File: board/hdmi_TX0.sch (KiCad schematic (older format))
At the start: 21 parts

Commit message: Update from the template.
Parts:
- CTX001, CTX002, CTX003, CTX004, CTX005, CTX006, CTX007, CTX008, CTX016, CTX017: value 100n -> 0.1uF
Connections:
- net HDMI_TX0_EQ0: now also PTX0.9 (P9); no longer PTX0.3 (P3)
- net HDMI_TX0_EQ1: now also PTX0.3 (P3); no longer PTX0.9 (P9)
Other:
- note added: "This sheet is generated from ../external/templates/\nDO NOT MODIFY!!!\n1620b96"
- note removed: "This sheet is generated from ../external/templates/\nDO NOT MODIFY!!!\nee70a4a"
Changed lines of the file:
@@
 LIBS:contrib
 LIBS:valves
-LIBS:pmod
+LIBS:pmod-conn_6x2
+LIBS:ma78l00
 LIBS:hdmi
 LIBS:ptn3363
-LIBS:ma78l00
-LIBS:pmod-conn_6x2
-LIBS:EEPROM
-LIBS:xc9140
-LIBS:reg710-dbv
-LIBS:pmod-hdmi-tx-cache
 EELAYER 25 0
 EELAYER END
 $Descr A3 16535 11693
 encoding utf-8
-Sheet 1 2
+Sheet 1 1
 Title ""
 Date ""
@@
 U 1 1 57C07746
 P 7450 5400
-AR Path="/57C07746" Ref="UTX0"  Part="1"
-AR Path="/5802F547/57C07746" Ref="UTX0"  Part="1"
 F 0 "UTX0" H 7100 6900 60  0000 C CNN
 F 1 "PTN3363" H 7700 3950 60  0000 C CNN
@@
 HDMIP_TX0_HPD
 $Comp
-L GND #PWR010
+L GND #PWR106
 U 1 1 57B7C214
 P 7450 7150
-F 0 "#PWR010" H 7450 6900 60  0001 C CNN
+F 0 "#PWR106" H 7450 6900 60  0001 C CNN
 F 1 "GND" H 7450 7000 60  0000 C CNN
 F 2 "" H 7450 7150 60  0000 C CNN
@@
 $EndComp
 $Comp
-L GND #PWR011
+L GND #PWR112
 U 1 1 57C0774B
 P 11600 6900
-F 0 "#PWR011" H 11600 6650 60  0001 C CNN
+F 0 "#PWR112" H 11600 6650 60  0001 C CNN
 F 1 "GND" H 11600 6750 60  0000 C CNN
 F 2 "" H 11600 6900 60  0000 C CNN
@@
 AR Path="/57C07751" Ref="RTX008"  Part="1"
 AR Path="/57C01383/57C07751" Ref="RTX003"  Part="1"
-AR Path="/5802F547/57C07751" Ref="RTX008"  Part="1"
 F 0 "RTX008" V 10700 4950 50  0000 C CNN
 F 1 "27K" V 10607 4951 50  0000 C CNN
@@
 AR Path="/57C07753" Ref="RTX002"  Part="1"
 AR Path="/57C01383/57C07753" Ref="RTX001"  Part="1"
-AR Path="/5802F547/57C07753" Ref="RTX002"  Part="1"
 F 0 "RTX002" V 3800 4400 50  0000 C CNN
 F 1 "2k2" V 3907 4401 50  0000 C CNN
@@
 AR Path="/57C07755" Ref="RTX001"  Part="1"
 AR Path="/57C01383/57C07755" Ref="RTX002"  Part="1"
-AR Path="/5802F547/57C07755" Ref="RTX001"  Part="1"
 F 0 "RTX001" V 4080 4400 50  0000 C CNN
 F 1 "2k2" V 4007 4401 50  0000 C CNN
@@
 	11750 4850 11600 4850
 Wire Wire Line
-	11600 4850 11600 6900
+	11600 4850 11600 5150
+Wire Wire Line
+	11600 5150 11600 5450
+Wire Wire Line
+	11600 5450 11600 5750
+Wire Wire Line
+	11600 5750 11600 6350
+Wire Wire Line
+	11600 6350 11600 6900
 Wire Wire Line
 	11750 5150 11600 5150
@@
 	6400 5800 6750 5800
 Wire Wire Line
-	8150 6600 9000 6600
+	8150 6600 8550 6600
+Wire Wire Line
+	8550 6600 9000 6600
 Wire Wire Line
 	8150 6400 9000 6400
 Wire Wire Line
-	7400 3750 7500 3750
-Wire Wire Line
-	7450 3200 7450 3750
+	7400 3750 7450 3750
+Wire Wire Line
+	7450 3750 7500 3750
+Wire Wire Line
+	7450 3750 7450 3200
 Connection ~ 7450 3750
 Wire Wire Line
@@
 Connection ~ 11600 6350
 Wire Wire Line
-	9800 5950 11750 5950
+	9800 5950 10600 5950
+Wire Wire Line
+	10600 5950 11750 5950
 Wire Wire Line
 	10600 5950 10600 5590
@@
 P 6300 4800
 F 0 "CTX001" V 6265 4840 30  0000 L CNN
-F 1 "100n" V 6270 4665 30  0000 L CNN
+F 1 "0.1uF" V 6270 4665 30  0000 L CNN
 F 2 "Capacitors_SMD:C_0402" H 6300 4800 60  0001 C CNN
 F 3 "" H 6300 4800 60  0000 C CNN
@@
 P 6300 4900
 F 0 "CTX002" V 6270 4940 30  0000 L CNN
-F 1 "100n" V 6270 4765 30  0000 L CNN
+F 1 "0.1uF" V 6270 4765 30  0000 L CNN
 F 2 "Capacitors_SMD:C_0402" H 6300 4900 60  0001 C CNN
 F 3 "" H 6300 4900 60  0000 C CNN
@@
 	4000 4100 4000 4250
 Wire Wire Line
-	3900 4100 4000 4100
+	3900 4100 3950 4100
+Wire Wire Line
+	3950 4100 4000 4100
 Text Label 3800 5900 2    60   ~ 0
 HDMIP_TX0_SCL
@@
 AR Path="/57C07769" Ref="RTX004"  Part="1"
 AR Path="/57C01383/57C07769" Ref="RTX004"  Part="1"
-AR Path="/5802F547/57C07769" Ref="RTX004"  Part="1"
 F 0 "RTX004" V 3800 5600 50  0000 C CNN
 F 1 "2k2" V 3907 5601 50  0000 C CNN
@@
 AR Path="/57B7FCE7" Ref="RTX005"  Part="1"
 AR Path="/57C01383/57B7FCE7" Ref="RTX005"  Part="1"
-AR Path="/5802F547/57B7FCE7" Ref="RTX005"  Part="1"
 F 0 "RTX005" V 4080 5600 50  0000 C CNN
 F 1 "2k2" V 4007 5601 50  0000 C CNN
@@
 AR Path="/57C0776D" Ref="RTX003"  Part="1"
 AR Path="/57C01383/57C0776D" Ref="RTX006"  Part="1"
-AR Path="/5802F547/57C0776D" Ref="RTX003"  Part="1"
 F 0 "RTX003" V 6580 6900 50  0000 C CNN
 F 1 "12k4" V 6507 6901 50  0000 C CNN
@@
 	6500 6300 6500 6750
 $Comp
-L GND #PWR012
+L GND #PWR104
 U 1 1 57C0776F
 P 6500 7150
-F 0 "#PWR012" H 6500 6900 60  0001 C CNN
+F 0 "#PWR104" H 6500 6900 60  0001 C CNN
 F 1 "GND" H 6500 7000 60  0000 C CNN
 F 2 "" H 6500 7150 60  0000 C CNN
@@
 	3900 5300 3900 5450
 Wire Wire Line
-	3900 5300 4000 5300
+	3900 5300 3950 5300
+Wire Wire Line
+	3950 5300 4000 5300
 Wire Wire Line
 	4000 5300 4000 5450
@@
 $EndComp
 $Comp
-L GND #PWR013
+L GND #PWR109
 U 1 1 57C07776
 P 8550 7150
-F 0 "#PWR013" H 8550 6900 60  0001 C CNN
+F 0 "#PWR109" H 8550 6900 60  0001 C CNN
 F 1 "GND" H 8550 7000 60  0000 C CNN
 F 2 "" H 8550 7150 60  0000 C CNN
@@
 AR Path="/57C07777" Ref="CTX017"  Part="1"
 AR Path="/57C01383/57C07777" Ref="CTX002"  Part="1"
-AR Path="/5802F547/57C07777" Ref="CTX017"  Part="1"
 F 0 "CTX017" H 8300 3750 30  0000 L CNN
-F 1 "100n" H 8300 3850 30  0000 L CNN
+F 1 "0.1uF" H 8300 3850 30  0000 L CNN
 F 2 "Capacitors_SMD:C_0402" H 8500 3850 60  0001 C CNN
 F 3 "" H 8500 3850 60  0000 C CNN
@@
 AR Path="/57C07779" Ref="CTX016"  Part="1"
 AR Path="/57C01383/57C07779" Ref="CTX001"  Part="1"
-AR Path="/5802F547/57C07779" Ref="CTX016"  Part="1"
 F 0 "CTX016" H 8350 3750 30  0000 L CNN
-F 1 "100n" H 8400 3850 30  0000 L CNN
+F 1 "0.1uF" H 8400 3850 30  0000 L CNN
 F 2 "Capacitors_SMD:C_0402" H 8300 3850 60  0001 C CNN
 F 3 "" H 8300 3850 60  0000 C CNN
@@
 $EndComp
 Wire Wire Line
-	8300 3600 8500 3600
+	8300 3600 8400 3600
+Wire Wire Line
+	8400 3600 8500 3600
 Wire Wire Line
 	8300 3600 8300 3700
@@
 	8300 4000 8300 4100
 Wire Wire Line
-	8300 4100 8500 4100
+	8300 4100 8400 4100
+Wire Wire Line
+	8400 4100 8500 4100
 Wire Wire Line
 	8500 4100 8500 4000
 $Comp
-L GND #PWR014
+L GND #PWR108
 U 1 1 57C0777E
 P 8400 4150
-F 0 "#PWR014" H 8400 3900 60  0001 C CNN
+F 0 "#PWR108" H 8400 3900 60  0001 C CNN
 F 1 "GND" H 8400 4000 60  0000 C CNN
 F 2 "" H 8400 4150 60  0000 C CNN
@@
 HDMI_TX0_SDA
 $Comp
-L GND #PWR015
+L GND #PWR101
 U 1 1 57C07784
 P 2255 6970
-F 0 "#PWR015" H 2255 6720 60  0001 C CNN
+F 0 "#PWR101" H 2255 6720 60  0001 C CNN
 F 1 "GND" H 2255 6820 60  0000 C CNN
 F 2 "" H 2255 6970 60  0000 C CNN
@@
 	6500 7050 6500 7150
 Text Notes 670  10960 0    197  ~ 39
-This sheet is generated from ../external/templates/\nDO NOT MODIFY!!!\nee70a4a
-Wire Wire Line
-	2255 6970 2865 6970
-Wire Wire Line
-	2725 7070 2865 7070
+This sheet is generated from ../external/templates/\nDO NOT MODIFY!!!\n1620b96
+Wire Wire Line
+	2255 6970 2325 6970
+Wire Wire Line
+	2325 6970 2865 6970
+Wire Wire Line
+	2725 7070 2770 7070
+Wire Wire Line
+	2770 7070 2865 7070
 Wire Wire Line
 	2865 6570 1885 6570
@@
 Text Label 4685 6870 2    60   ~ 0
 HDMI_TX0_DDET
-Text Label 1885 6770 0    60   ~ 0
+Text Label 4685 6770 2    60   ~ 0
 HDMI_TX0_EQ1
 Text Label 1885 6870 0    60   ~ 0
@@
 Wire Wire Line
 	4685 6570 3665 6570
-Text Label 4685 6770 2    60   ~ 0
+Text Label 1885 6770 0    60   ~ 0
 HDMI_TX0_EQ0
 $Comp
@@
 P 6300 5100
 F 0 "CTX003" V 6265 5140 30  0000 L CNN
-F 1 "100n" V 6270 4965 30  0000 L CNN
+F 1 "0.1uF" V 6270 4965 30  0000 L CNN
 F 2 "Capacitors_SMD:C_0402" H 6300 5100 60  0001 C CNN
 F 3 "" H 6300 5100 60  0000 C CNN
@@
 P 6300 5200
 F 0 "CTX004" V 6270 5240 30  0000 L CNN
-F 1 "100n" V 6270 5065 30  0000 L CNN
+F 1 "0.1uF" V 6270 5065 30  0000 L CNN
 F 2 "Capacitors_SMD:C_0402" H 6300 5200 60  0001 C CNN
 F 3 "" H 6300 5200 60  0000 C CNN
@@
 P 6300 5400
 F 0 "CTX005" V 6265 5440 30  0000 L CNN
-F 1 "100n" V 6270 5265 30  0000 L CNN
+F 1 "0.1uF" V 6270 5265 30  0000 L CNN
 F 2 "Capacitors_SMD:C_0402" H 6300 5400 60  0001 C CNN
 F 3 "" H 6300 5400 60  0000 C CNN
@@
 P 6300 5500
 F 0 "CTX006" V 6270 5540 30  0000 L CNN
-F 1 "100n" V 6270 5365 30  0000 L CNN
+F 1 "0.1uF" V 6270 5365 30  0000 L CNN
 F 2 "Capacitors_SMD:C_0402" H 6300 5500 60  0001 C CNN
 F 3 "" H 6300 5500 60  0000 C CNN
@@
 P 6300 5700
 F 0 "CTX007" V 6265 5740 30  0000 L CNN
-F 1 "100n" V 6270 5565 30  0000 L CNN
+F 1 "0.1uF" V 6270 5565 30  0000 L CNN
 F 2 "Capacitors_SMD:C_0402" H 6300 5700 60  0001 C CNN
 F 3 "" H 6300 5700 60  0000 C CNN
@@
 P 6300 5800
 F 0 "CTX008" V 6270 5840 30  0000 L CNN
-F 1 "100n" V 6270 5665 30  0000 L CNN
+F 1 "0.1uF" V 6270 5665 30  0000 L CNN
 F 2 "Capacitors_SMD:C_0402" H 6300 5800 60  0001 C CNN
 F 3 "" H 6300 5800 60  0000 C CNN
@@
 Text GLabel 7025 3200 0    60   Input ~ 0
 VCC3V3
+Wire Wire Line
+	7025 3200 7375 3200
 $Comp
 L PMOD-CONN_6X2 PTX0
@@
 	-1   0    0    -1
 $EndComp
+Wire Wire Line
+	8400 3600 8400 3515
+Text Label 8400 3515 0    60   ~ 0
+VCC3V3
 Text Label 10600 4450 0    60   ~ 0
 VCC3V3
-Text Label 8400 3200 2    60   ~ 0
+Text Label 7375 3200 2    60   ~ 0
 VCC3V3
 Text Label 3950 4050 0    60   ~ 0
@@
 TX05V0
 Wire Wire Line
-	7025 3200 8400 3200
+	7025 3200 7450 3200
+Wire Wire Line
+	7450 3200 8400 3200
 Wire Wire Line
 	8400 3200 8400 3600

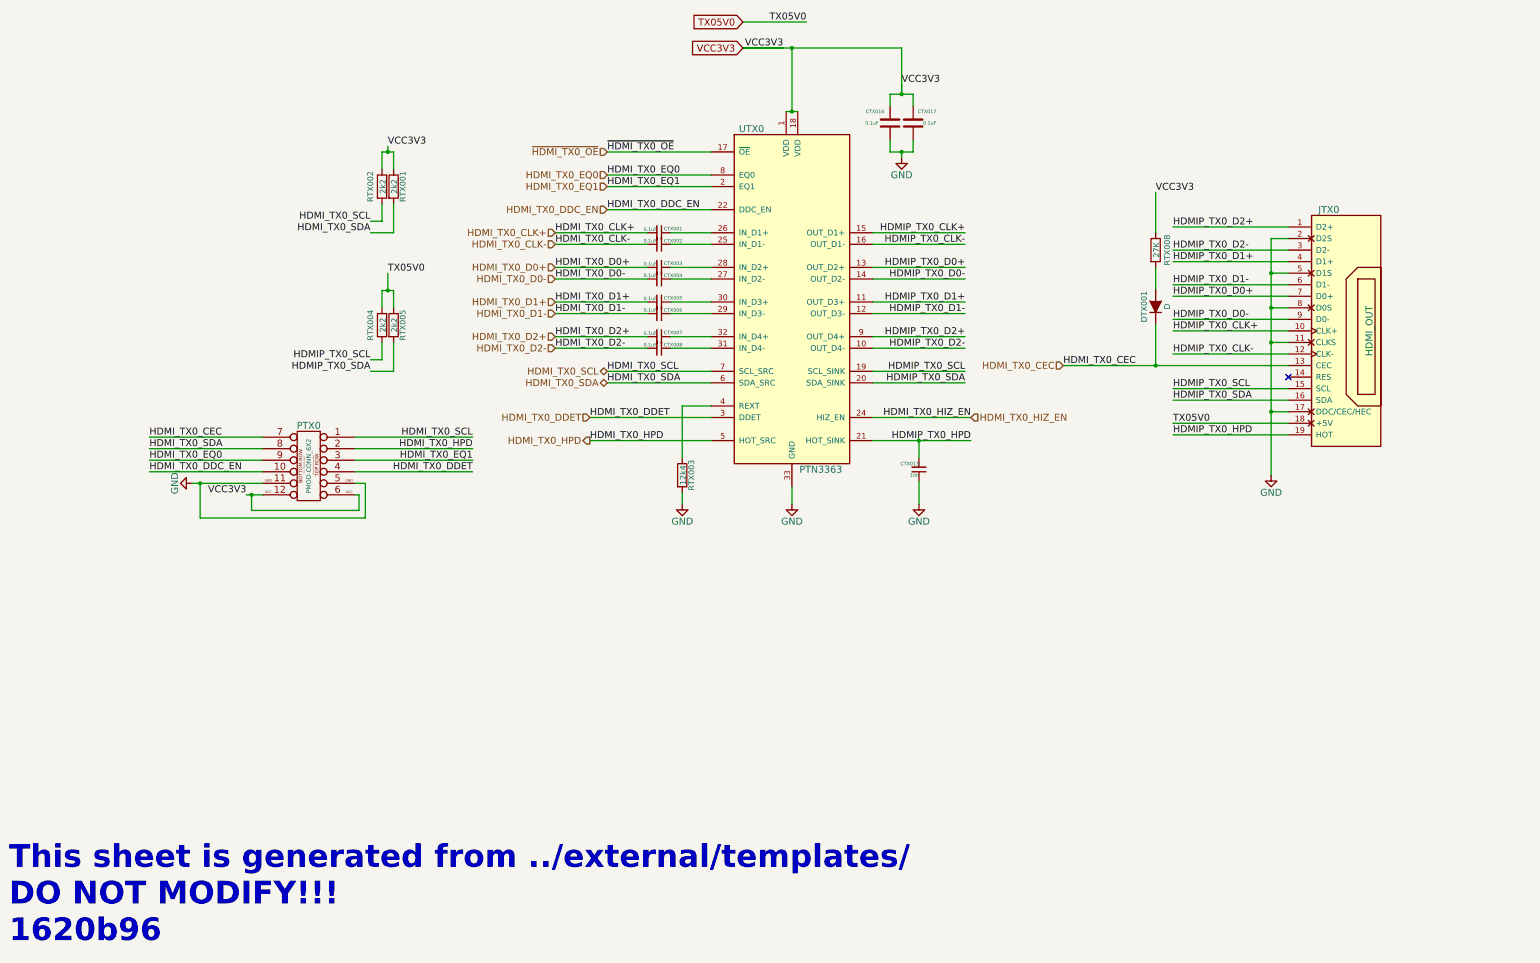
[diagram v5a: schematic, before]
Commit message: Updating the PCB a little.
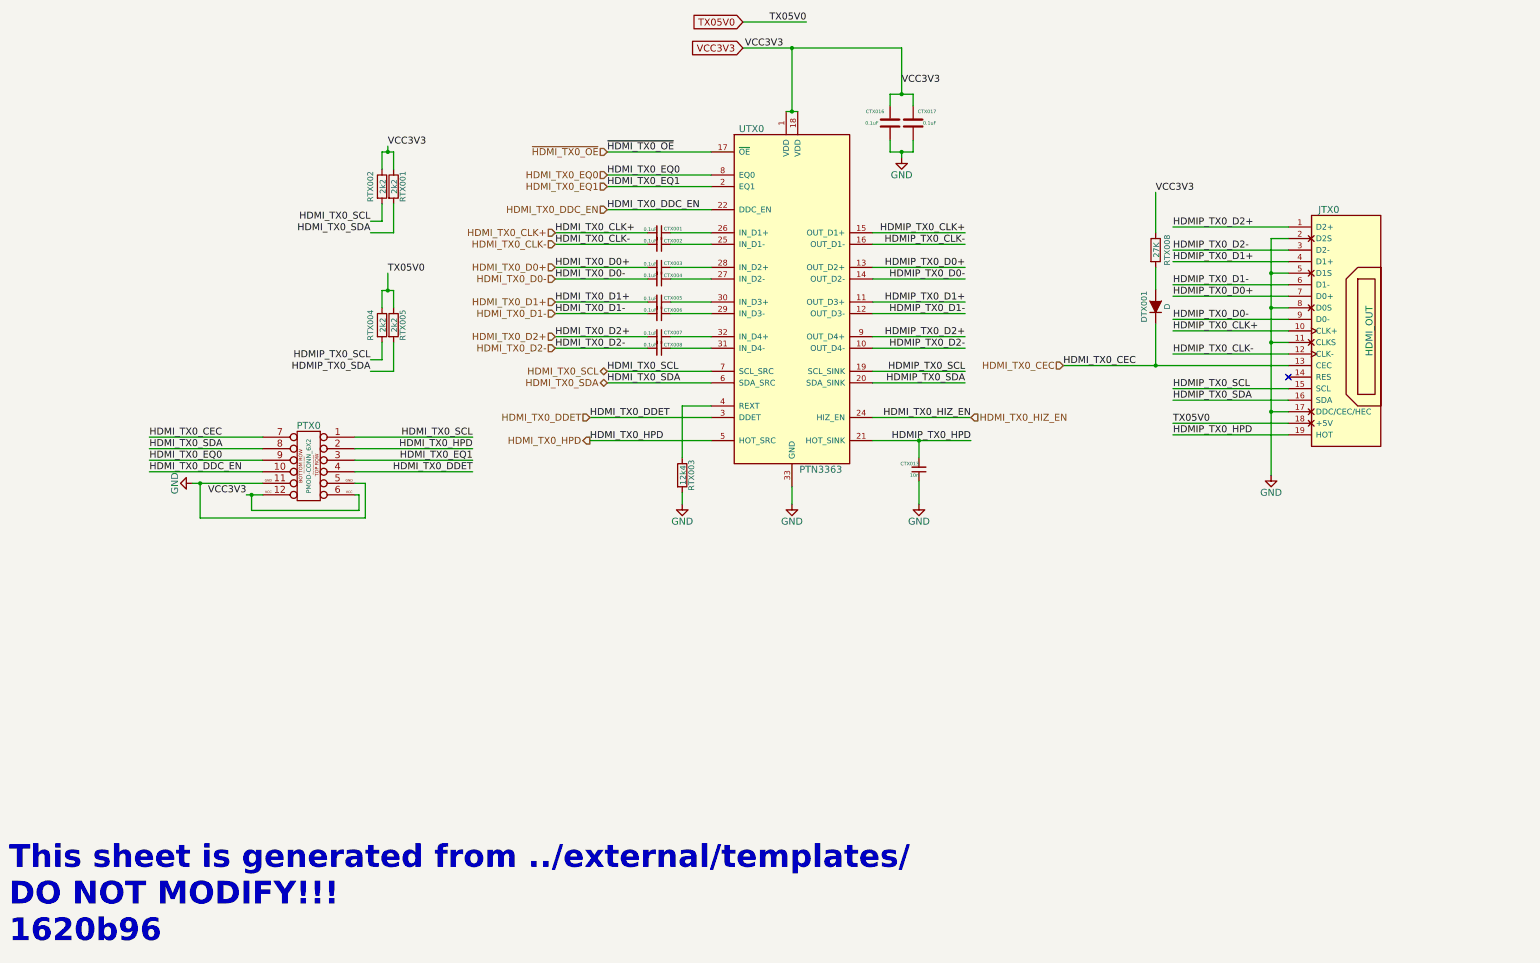
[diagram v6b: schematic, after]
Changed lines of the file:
@@
 LIBS:contrib
 LIBS:valves
-LIBS:pmod-conn_6x2
-LIBS:ma78l00
+LIBS:pmod
 LIBS:hdmi
 LIBS:ptn3363
+LIBS:ma78l00
+LIBS:pmod-conn_6x2
+LIBS:EEPROM
+LIBS:xc9140
+LIBS:reg710-dbv
+LIBS:pmod-hdmi-tx-cache
 EELAYER 25 0
 EELAYER END
 $Descr A3 16535 11693
 encoding utf-8
-Sheet 1 1
+Sheet 2 2
 Title ""
 Date ""
@@
 HDMIP_TX0_HPD
 $Comp
-L GND #PWR106
+L GND #PWR010
 U 1 1 57B7C214
 P 7450 7150
-F 0 "#PWR106" H 7450 6900 60  0001 C CNN
+F 0 "#PWR010" H 7450 6900 60  0001 C CNN
 F 1 "GND" H 7450 7000 60  0000 C CNN
 F 2 "" H 7450 7150 60  0000 C CNN
@@
 $EndComp
 $Comp
-L GND #PWR112
+L GND #PWR011
 U 1 1 57C0774B
 P 11600 6900
-F 0 "#PWR112" H 11600 6650 60  0001 C CNN
+F 0 "#PWR011" H 11600 6650 60  0001 C CNN
 F 1 "GND" H 11600 6750 60  0000 C CNN
 F 2 "" H 11600 6900 60  0000 C CNN
@@
 AR Path="/57C07751" Ref="RTX008"  Part="1"
 AR Path="/57C01383/57C07751" Ref="RTX003"  Part="1"
+AR Path="/5802F547/57C07751" Ref="RTX008"  Part="1"
 F 0 "RTX008" V 10700 4950 50  0000 C CNN
 F 1 "27K" V 10607 4951 50  0000 C CNN
@@
 AR Path="/57C07753" Ref="RTX002"  Part="1"
 AR Path="/57C01383/57C07753" Ref="RTX001"  Part="1"
+AR Path="/5802F547/57C07753" Ref="RTX002"  Part="1"
 F 0 "RTX002" V 3800 4400 50  0000 C CNN
 F 1 "2k2" V 3907 4401 50  0000 C CNN
@@
 AR Path="/57C07755" Ref="RTX001"  Part="1"
 AR Path="/57C01383/57C07755" Ref="RTX002"  Part="1"
+AR Path="/5802F547/57C07755" Ref="RTX001"  Part="1"
 F 0 "RTX001" V 4080 4400 50  0000 C CNN
 F 1 "2k2" V 4007 4401 50  0000 C CNN
@@
 	11750 4850 11600 4850
 Wire Wire Line
-	11600 4850 11600 5150
-Wire Wire Line
-	11600 5150 11600 5450
-Wire Wire Line
-	11600 5450 11600 5750
-Wire Wire Line
-	11600 5750 11600 6350
-Wire Wire Line
-	11600 6350 11600 6900
+	11600 4850 11600 6900
 Wire Wire Line
 	11750 5150 11600 5150
@@
 	6400 5800 6750 5800
 Wire Wire Line
-	8150 6600 8550 6600
-Wire Wire Line
-	8550 6600 9000 6600
+	8150 6600 9000 6600
 Wire Wire Line
 	8150 6400 9000 6400
 Wire Wire Line
-	7400 3750 7450 3750
-Wire Wire Line
-	7450 3750 7500 3750
-Wire Wire Line
-	7450 3750 7450 3200
+	7400 3750 7500 3750
+Wire Wire Line
+	7450 3200 7450 3750
 Connection ~ 7450 3750
 Wire Wire Line
@@
 Connection ~ 11600 6350
 Wire Wire Line
-	9800 5950 10600 5950
-Wire Wire Line
-	10600 5950 11750 5950
+	9800 5950 11750 5950
 Wire Wire Line
 	10600 5950 10600 5590
@@
 	4000 4100 4000 4250
 Wire Wire Line
-	3900 4100 3950 4100
-Wire Wire Line
-	3950 4100 4000 4100
+	3900 4100 4000 4100
 Text Label 3800 5900 2    60   ~ 0
 HDMIP_TX0_SCL
@@
 AR Path="/57C07769" Ref="RTX004"  Part="1"
 AR Path="/57C01383/57C07769" Ref="RTX004"  Part="1"
+AR Path="/5802F547/57C07769" Ref="RTX004"  Part="1"
 F 0 "RTX004" V 3800 5600 50  0000 C CNN
 F 1 "2k2" V 3907 5601 50  0000 C CNN
@@
 AR Path="/57B7FCE7" Ref="RTX005"  Part="1"
 AR Path="/57C01383/57B7FCE7" Ref="RTX005"  Part="1"
+AR Path="/5802F547/57B7FCE7" Ref="RTX005"  Part="1"
 F 0 "RTX005" V 4080 5600 50  0000 C CNN
 F 1 "2k2" V 4007 5601 50  0000 C CNN
@@
 AR Path="/57C0776D" Ref="RTX003"  Part="1"
 AR Path="/57C01383/57C0776D" Ref="RTX006"  Part="1"
+AR Path="/5802F547/57C0776D" Ref="RTX003"  Part="1"
 F 0 "RTX003" V 6580 6900 50  0000 C CNN
 F 1 "12k4" V 6507 6901 50  0000 C CNN
@@
 	6500 6300 6500 6750
 $Comp
-L GND #PWR104
+L GND #PWR012
 U 1 1 57C0776F
 P 6500 7150
-F 0 "#PWR104" H 6500 6900 60  0001 C CNN
+F 0 "#PWR012" H 6500 6900 60  0001 C CNN
 F 1 "GND" H 6500 7000 60  0000 C CNN
 F 2 "" H 6500 7150 60  0000 C CNN
@@
 	3900 5300 3900 5450
 Wire Wire Line
-	3900 5300 3950 5300
-Wire Wire Line
-	3950 5300 4000 5300
+	3900 5300 4000 5300
 Wire Wire Line
 	4000 5300 4000 5450
@@
 $EndComp
 $Comp
-L GND #PWR109
+L GND #PWR013
 U 1 1 57C07776
 P 8550 7150
-F 0 "#PWR109" H 8550 6900 60  0001 C CNN
+F 0 "#PWR013" H 8550 6900 60  0001 C CNN
 F 1 "GND" H 8550 7000 60  0000 C CNN
 F 2 "" H 8550 7150 60  0000 C CNN
@@
 AR Path="/57C07777" Ref="CTX017"  Part="1"
 AR Path="/57C01383/57C07777" Ref="CTX002"  Part="1"
+AR Path="/5802F547/57C07777" Ref="CTX017"  Part="1"
 F 0 "CTX017" H 8300 3750 30  0000 L CNN
 F 1 "0.1uF" H 8300 3850 30  0000 L CNN
@@
 AR Path="/57C07779" Ref="CTX016"  Part="1"
 AR Path="/57C01383/57C07779" Ref="CTX001"  Part="1"
+AR Path="/5802F547/57C07779" Ref="CTX016"  Part="1"
 F 0 "CTX016" H 8350 3750 30  0000 L CNN
 F 1 "0.1uF" H 8400 3850 30  0000 L CNN
@@
 $EndComp
 Wire Wire Line
-	8300 3600 8400 3600
-Wire Wire Line
-	8400 3600 8500 3600
+	8300 3600 8500 3600
 Wire Wire Line
 	8300 3600 8300 3700
@@
 	8300 4000 8300 4100
 Wire Wire Line
-	8300 4100 8400 4100
-Wire Wire Line
-	8400 4100 8500 4100
+	8300 4100 8500 4100
 Wire Wire Line
 	8500 4100 8500 4000
 $Comp
-L GND #PWR108
+L GND #PWR014
 U 1 1 57C0777E
 P 8400 4150
-F 0 "#PWR108" H 8400 3900 60  0001 C CNN
+F 0 "#PWR014" H 8400 3900 60  0001 C CNN
 F 1 "GND" H 8400 4000 60  0000 C CNN
 F 2 "" H 8400 4150 60  0000 C CNN
@@
 HDMI_TX0_SDA
 $Comp
-L GND #PWR101
+L GND #PWR015
 U 1 1 57C07784
 P 2255 6970
-F 0 "#PWR101" H 2255 6720 60  0001 C CNN
+F 0 "#PWR015" H 2255 6720 60  0001 C CNN
 F 1 "GND" H 2255 6820 60  0000 C CNN
 F 2 "" H 2255 6970 60  0000 C CNN
@@
 This sheet is generated from ../external/templates/\nDO NOT MODIFY!!!\n1620b96
 Wire Wire Line
-	2255 6970 2325 6970
-Wire Wire Line
-	2325 6970 2865 6970
-Wire Wire Line
-	2725 7070 2770 7070
-Wire Wire Line
-	2770 7070 2865 7070
+	2255 6970 2865 6970
+Wire Wire Line
+	2725 7070 2865 7070
 Wire Wire Line
 	2865 6570 1885 6570
@@
 VCC3V3
 Wire Wire Line
-	7025 3200 7375 3200
+	7025 3200 8400 3200
 $Comp
 L PMOD-CONN_6X2 PTX0
@@
 $EndComp
 Wire Wire Line
-	8400 3600 8400 3515
+	8400 3200 8400 3600
 Text Label 8400 3515 0    60   ~ 0
 VCC3V3
@@
 Text GLabel 7025 2975 0    60   Input ~ 0
 TX05V0
-Wire Wire Line
-	7025 3200 7450 3200
-Wire Wire Line
-	7450 3200 8400 3200
-Wire Wire Line
-	8400 3200 8400 3600
 Connection ~ 7450 3200
 Wire Wire Line
